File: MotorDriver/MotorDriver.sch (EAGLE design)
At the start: 85 parts, among them IC1 DRV8320RSRHAR, IC2 MAX3051ESA+, IC3 TPD4S014DSQR, J1 J_USB_MICROAB_HIROSE_ZX62-AB-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, J2 SM03B-ZESS-TB, Q1 BUK7Y7R8-80EX, Q2 BUK7Y7R8-80EX, Q3 BUK7Y7R8-80EX, Q4 BUK7Y7R8-80EX, Q5 BUK7Y7R8-80EX, Q6 BUK7Y7R8-80EX, U1 LPC1549JBD48, U2 ADCMP350YKSZ, U3 MCP1700T-33, U4 ADR5041, Y1 FA238V

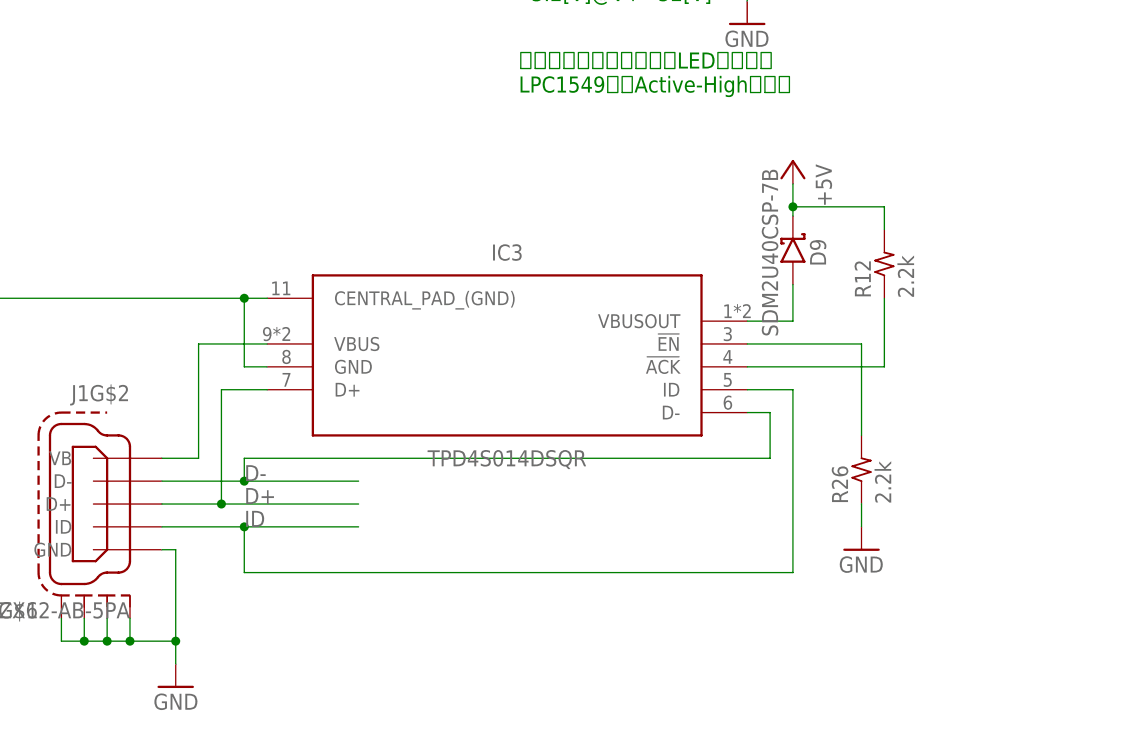
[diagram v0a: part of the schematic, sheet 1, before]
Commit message: デバイス側で`id`を使ってUSBの接続を検出するのは不可能なので保護ICの`!ack`を使うように変更
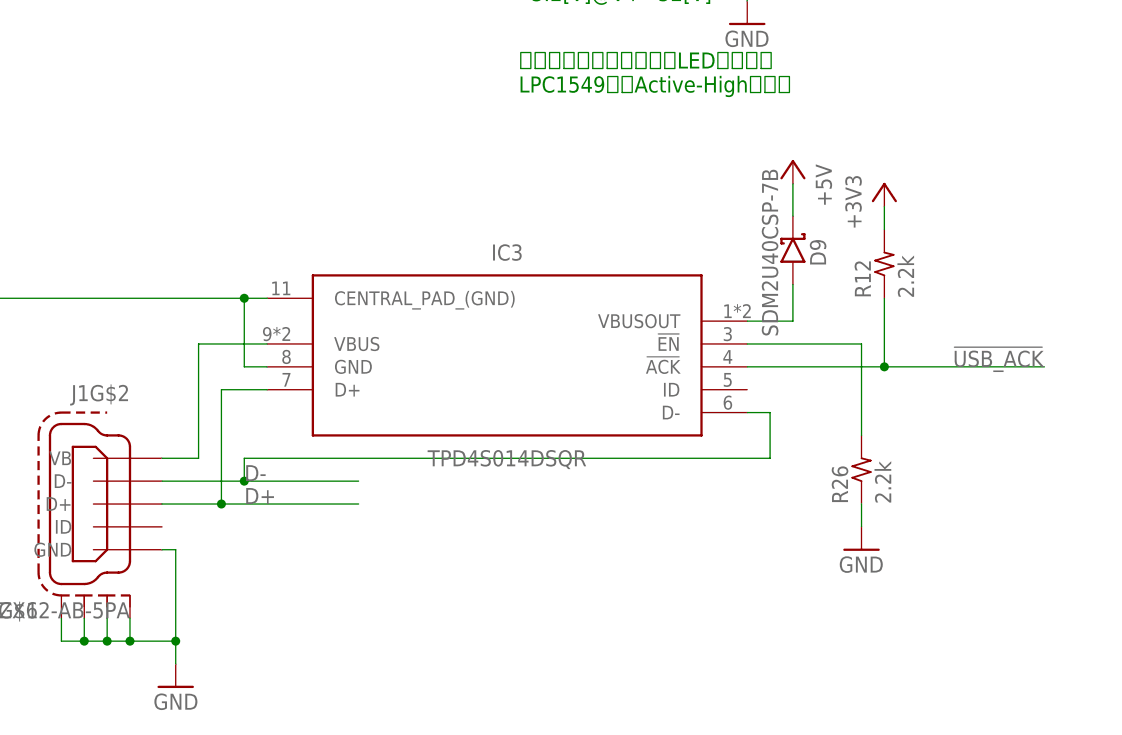
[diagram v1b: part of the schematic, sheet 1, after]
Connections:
- removed net ID: IC3.ID, J1G$2.ID, U1.PIO0_14/ADC1_7/SCT1_OUT5
- removed net N$29: IC3.!ACK, R12.1
- new net !USB_ACK: IC3.!ACK, R12.1, U1.PIO0_14/ADC1_7/SCT1_OUT5
- net +3V3: now also R12.2
- net +5V: no longer R12.2
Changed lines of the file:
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@@
 <?xml version="1.0" encoding="utf-8"?>
 <!DOCTYPE eagle SYSTEM "eagle.dtd">
-<eagle version="8.4.3">
+<eagle version="8.6.3">
 <drawing>
 <settings>
@@
 <part name="R12" library="MotorDriver" library_urn="urn:adsk.eagle:library:1073580" deviceset="R" device="1005" package3d_urn="urn:adsk.eagle:package:1073655/2" value="2.2k"/>
 <part name="R26" library="MotorDriver" library_urn="urn:adsk.eagle:library:1073580" deviceset="R" device="1005" package3d_urn="urn:adsk.eagle:package:1073655/2" value="2.2k"/>
+<part name="+3V12" library="supply1" deviceset="+3V3" device=""/>
 </parts>
 <sheets>
@@
 <instance part="R12" gate="G$1" x="-5.08" y="-35.56" rot="R90"/>
 <instance part="R26" gate="G$1" x="-7.62" y="-58.42" rot="R90"/>
+<instance part="+3V12" gate="G$1" x="-5.08" y="-27.94"/>
 </instances>
 <busses>
@@
 <wire x1="-50.8" y1="22.86" x2="-50.8" y2="25.4" width="0.1524" layer="91"/>
 </segment>
+<segment>
+<pinref part="R12" gate="G$1" pin="2"/>
+<wire x1="-5.08" y1="-33.02" x2="-5.08" y2="-30.48" width="0.1524" layer="91"/>
+<pinref part="+3V12" gate="G$1" pin="+3V3"/>
+</segment>
 </net>
 <net name="VREF" class="0">
@@
 <pinref part="+P3" gate="1" pin="+5V"/>
 <pinref part="D9" gate="G$1" pin="K"/>
-<wire x1="-15.24" y1="-31.496" x2="-15.24" y2="-30.48" width="0.1524" layer="91"/>
-<pinref part="R12" gate="G$1" pin="2"/>
-<wire x1="-15.24" y1="-30.48" x2="-15.24" y2="-27.94" width="0.1524" layer="91"/>
-<wire x1="-5.08" y1="-33.02" x2="-5.08" y2="-30.48" width="0.1524" layer="91"/>
-<wire x1="-5.08" y1="-30.48" x2="-15.24" y2="-30.48" width="0.1524" layer="91"/>
-<junction x="-15.24" y="-30.48"/>
+<wire x1="-15.24" y1="-31.496" x2="-15.24" y2="-27.94" width="0.1524" layer="91"/>
 </segment>
 </net>
@@
 </segment>
 </net>
-<net name="ID" class="0">
-<segment>
-<pinref part="J1" gate="G$2" pin="ID"/>
-<wire x1="-85.344" y1="-66.04" x2="-76.2" y2="-66.04" width="0.1524" layer="91"/>
-<label x="-76.2" y="-66.04" size="1.778" layer="95"/>
-<pinref part="IC3" gate="G$1" pin="ID"/>
-<wire x1="-76.2" y1="-66.04" x2="-63.5" y2="-66.04" width="0.1524" layer="91"/>
-<wire x1="-20.32" y1="-50.8" x2="-15.24" y2="-50.8" width="0.1524" layer="91"/>
-<wire x1="-15.24" y1="-50.8" x2="-15.24" y2="-71.12" width="0.1524" layer="91"/>
-<wire x1="-15.24" y1="-71.12" x2="-76.2" y2="-71.12" width="0.1524" layer="91"/>
-<wire x1="-76.2" y1="-71.12" x2="-76.2" y2="-66.04" width="0.1524" layer="91"/>
-<junction x="-76.2" y="-66.04"/>
-</segment>
-</net>
 <net name="N$23" class="0">
 <segment>
@@
 </segment>
 </net>
-<net name="N$29" class="0">
+<net name="!USB_ACK" class="0">
 <segment>
 <pinref part="IC3" gate="G$1" pin="!ACK"/>
@@
 <wire x1="-20.32" y1="-48.26" x2="-5.08" y2="-48.26" width="0.1524" layer="91"/>
 <wire x1="-5.08" y1="-48.26" x2="-5.08" y2="-40.64" width="0.1524" layer="91"/>
+<wire x1="-5.08" y1="-48.26" x2="12.7" y2="-48.26" width="0.1524" layer="91"/>
+<junction x="-5.08" y="-48.26"/>
+<label x="2.54" y="-48.26" size="1.778" layer="95"/>
 </segment>
 </net>
@@
 </segment>
 </net>
-<net name="ID" class="0">
+<net name="FUSE" class="0">
+<segment>
+<pinref part="U1" gate="G$1" pin="SWDIO/PIO0_20/SCT1_OUT6/TMS"/>
+<wire x1="93.98" y1="93.98" x2="109.22" y2="93.98" width="0.1524" layer="91"/>
+<label x="104.14" y="93.98" size="1.778" layer="95"/>
+</segment>
+</net>
+<net name="!USB_ACK" class="0">
 <segment>
 <pinref part="U1" gate="G$1" pin="PIO0_14/ADC1_7/SCT1_OUT5"/>
@@
 </segment>
 </net>
-<net name="FUSE" class="0">
-<segment>
-<pinref part="U1" gate="G$1" pin="SWDIO/PIO0_20/SCT1_OUT6/TMS"/>
-<wire x1="93.98" y1="93.98" x2="109.22" y2="93.98" width="0.1524" layer="91"/>
-<label x="104.14" y="93.98" size="1.778" layer="95"/>
-</segment>
-</net>

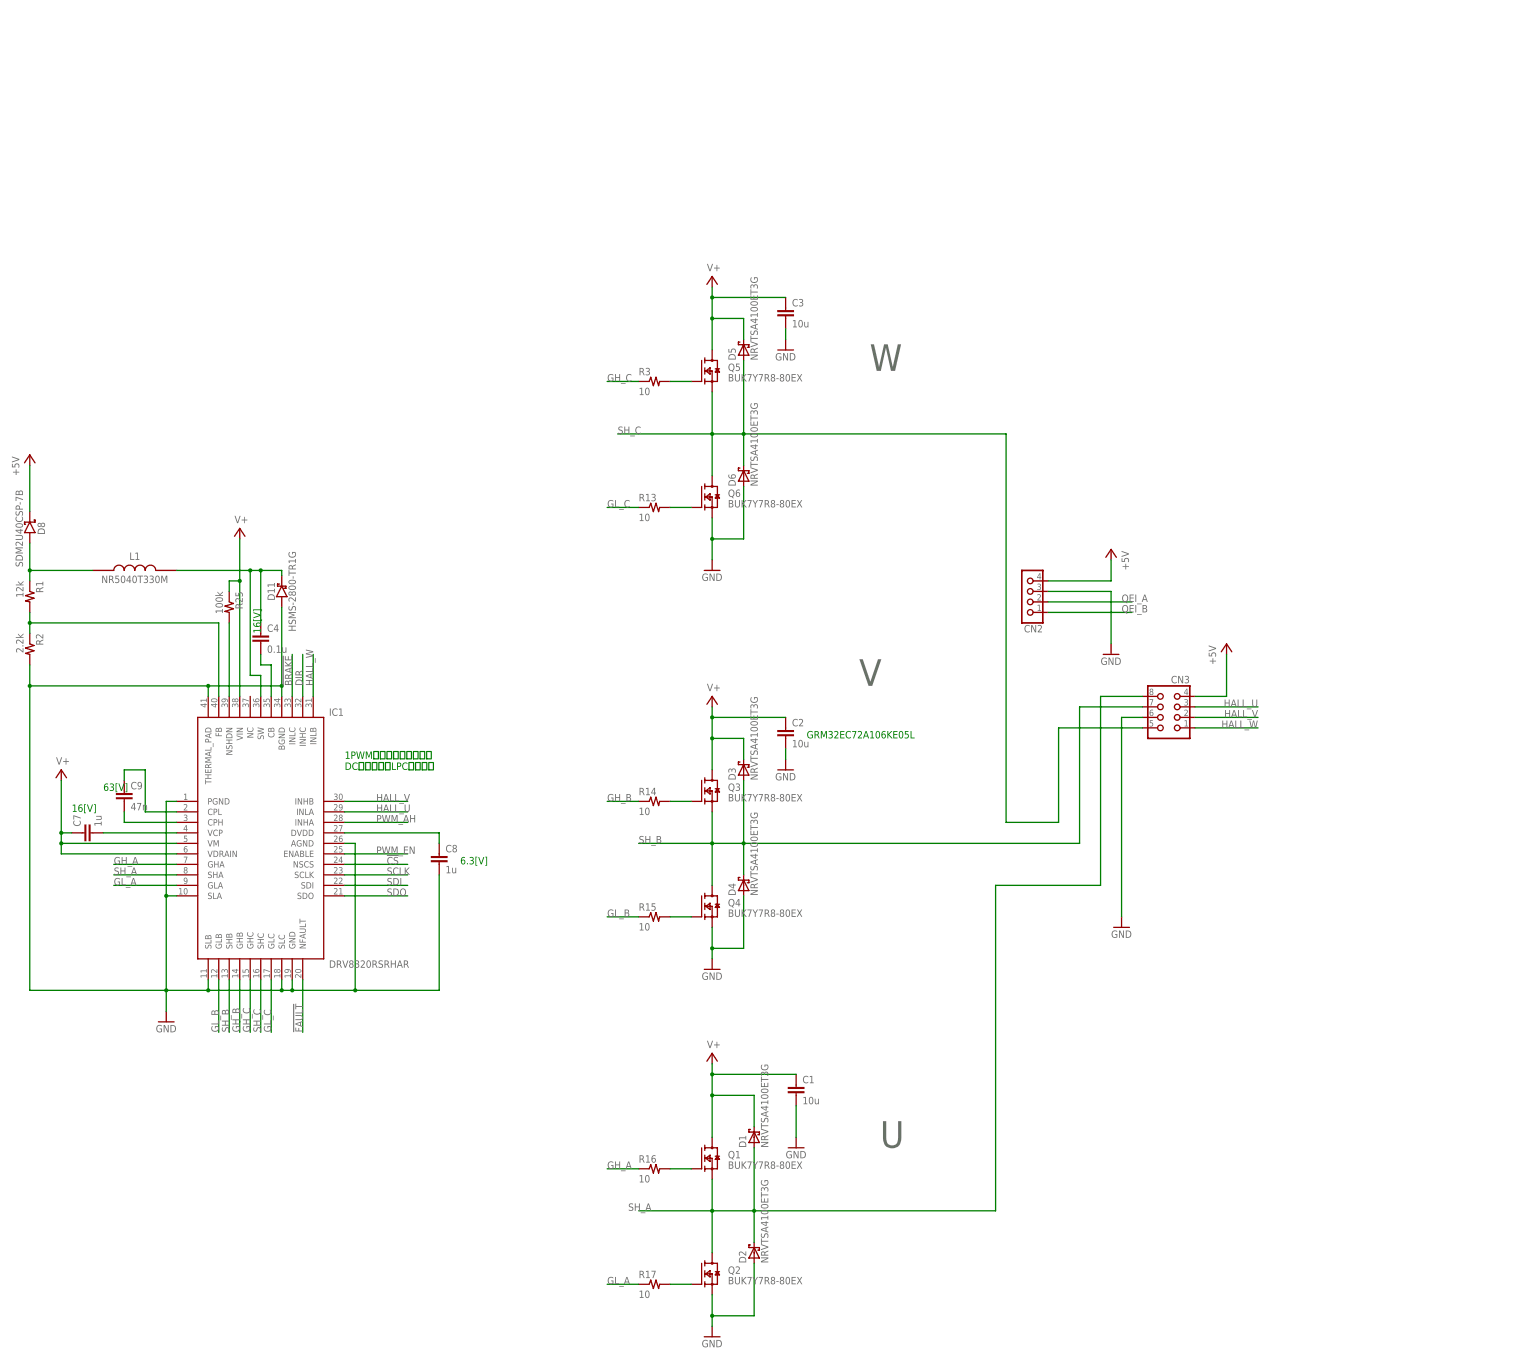
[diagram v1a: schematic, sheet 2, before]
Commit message: [fix]USB-ACKのプルアップ抵抗の変更とコメントの整理
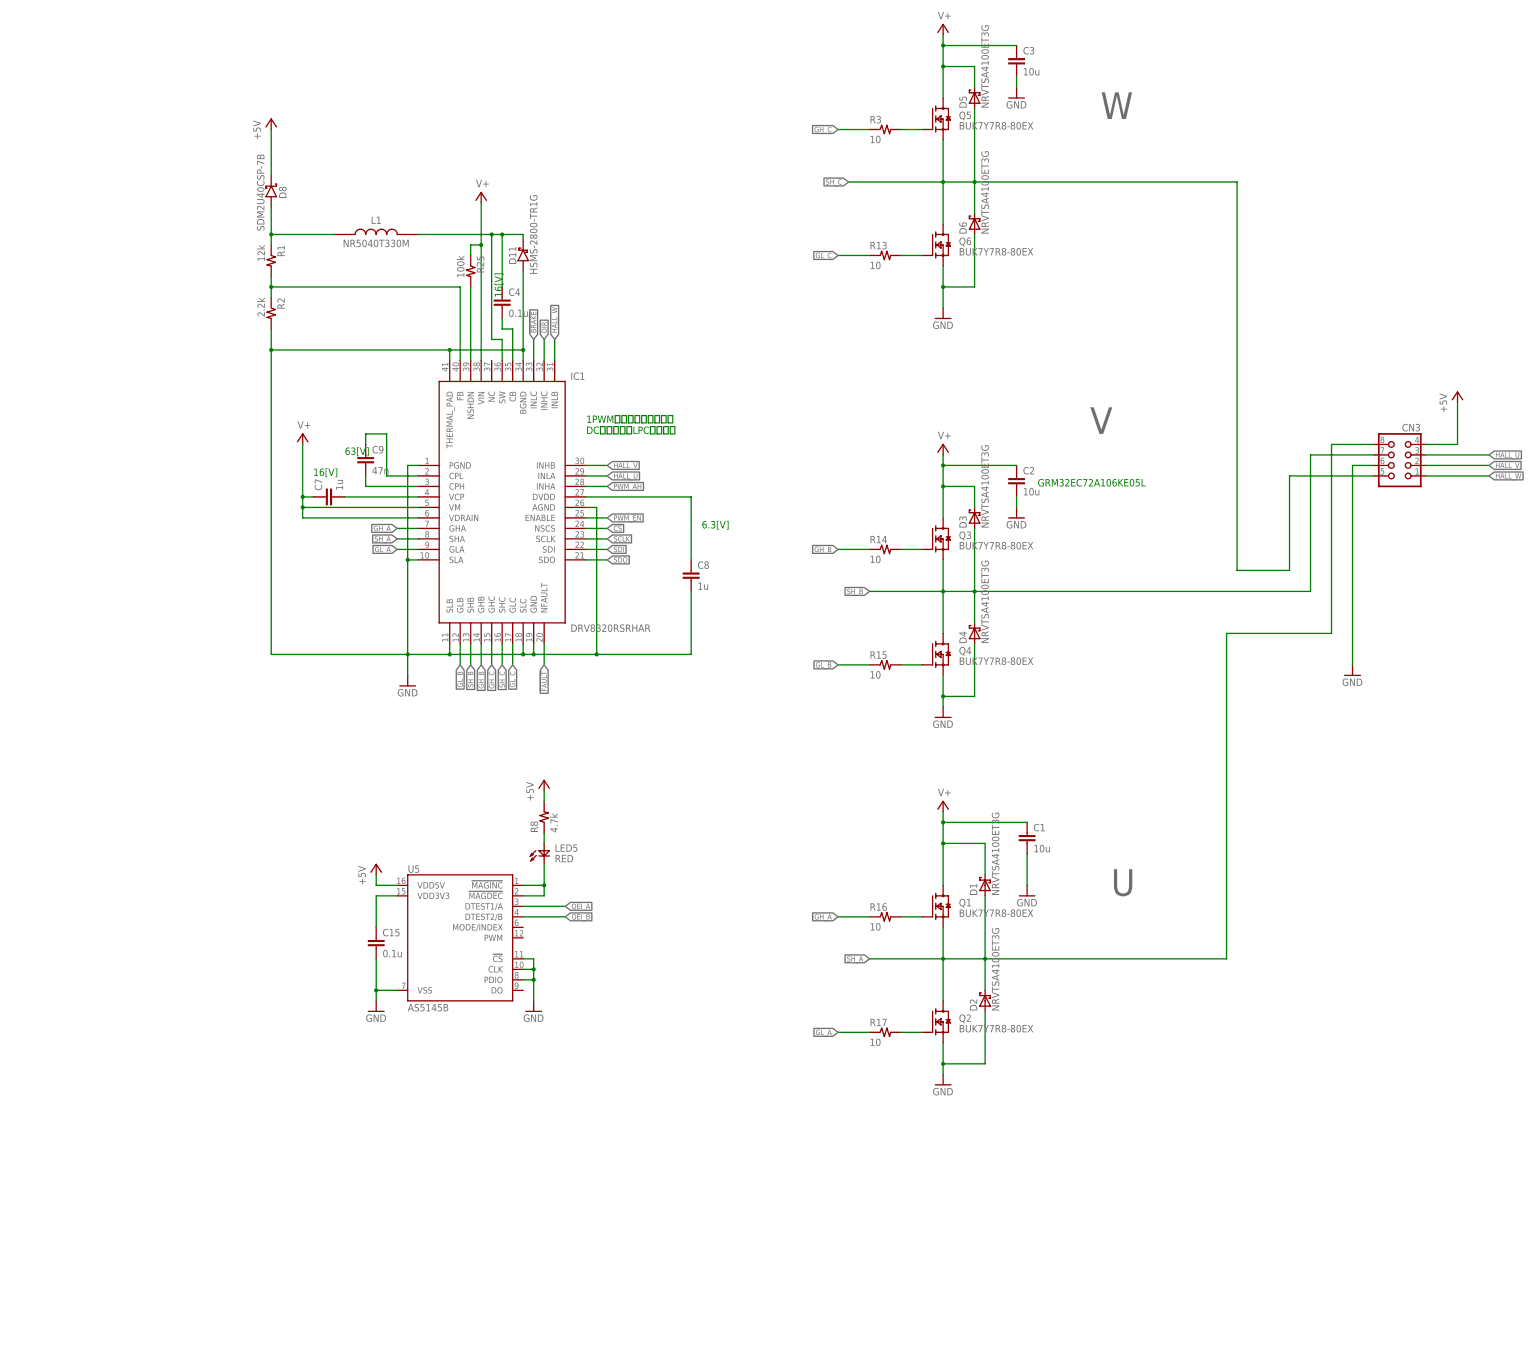
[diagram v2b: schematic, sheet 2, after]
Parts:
- removed CN2: (no value), con-Molex:53375-0410
- added C15: 0.1u, MotorDriver:C1005
- added C16: 22u, Passive:CPOLS-6.3
- added LED5: RED, MotorDriver:LED1608
- added R8: 4.7k, MotorDriver:R1005
- added U5: AS5145B, ic-ams:AS5145B
- D10: value SMAJ60A -> SMAJ54A
- F1: value 15 -> 20
- LED0, LED3: value (none) -> RED
- LED1: value (none) -> GREEN
- LED2: value (none) -> WHITE
- R12: value 2.2k -> 10k
- R18: value (none) -> 10k
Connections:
- new net N$29: C15.1, U5.VDD3V3
- new net N$30: LED5.K, U5.!MAGDEC, U5.!MAGINC
- new net N$32: LED5.A, R8.1
- net +5V: now also R8.2, U5.VDD5V; no longer CN2.4
- net GND: now also C15.2, C16.N, U5.!CS, U5.CLK, U5.PDIO, U5.VSS; no longer CN2.3
- net QEI_A: now also U5.DTEST1/A; no longer CN2.2
- net QEI_B: now also U5.DTEST2/B; no longer CN2.1
- net V+: now also C16.P
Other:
- note added: "ヒューズが切れていたらLEDが点灯 LPC1549にActive-Highで入力"
- note removed: "ヒューズが切れていたらLEDが切れる LPC1549のｍActive-Highで入力"
- note removed: "電源端子間はツェナーで60[V]までに制限"
- moved on the sheet: C1, C10, C11, C12, C13, C14, C19, C2, C20, C22, C23, C24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
